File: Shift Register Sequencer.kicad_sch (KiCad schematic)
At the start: 103 parts, among them J1 Gate IN, J10 Step 4, J11 Step C, J12 Step 5, J13 Step F, J14 Step 0-F, J2 Step 0, J3 Step 6, J4 Step 1, J5 Step 7, J6 Step 2, J7 Step 8, J8 Step 3, J9 Step A, Q1 2N3904, Q2 2N3904, SW1 oneShot/continous, SW2 oneShot/continous, U1 4070, U2 SN74HC595N, U3 SN74HC595N, U4 TL072, U5 CD4050, U6 CD4050, U7 TL072

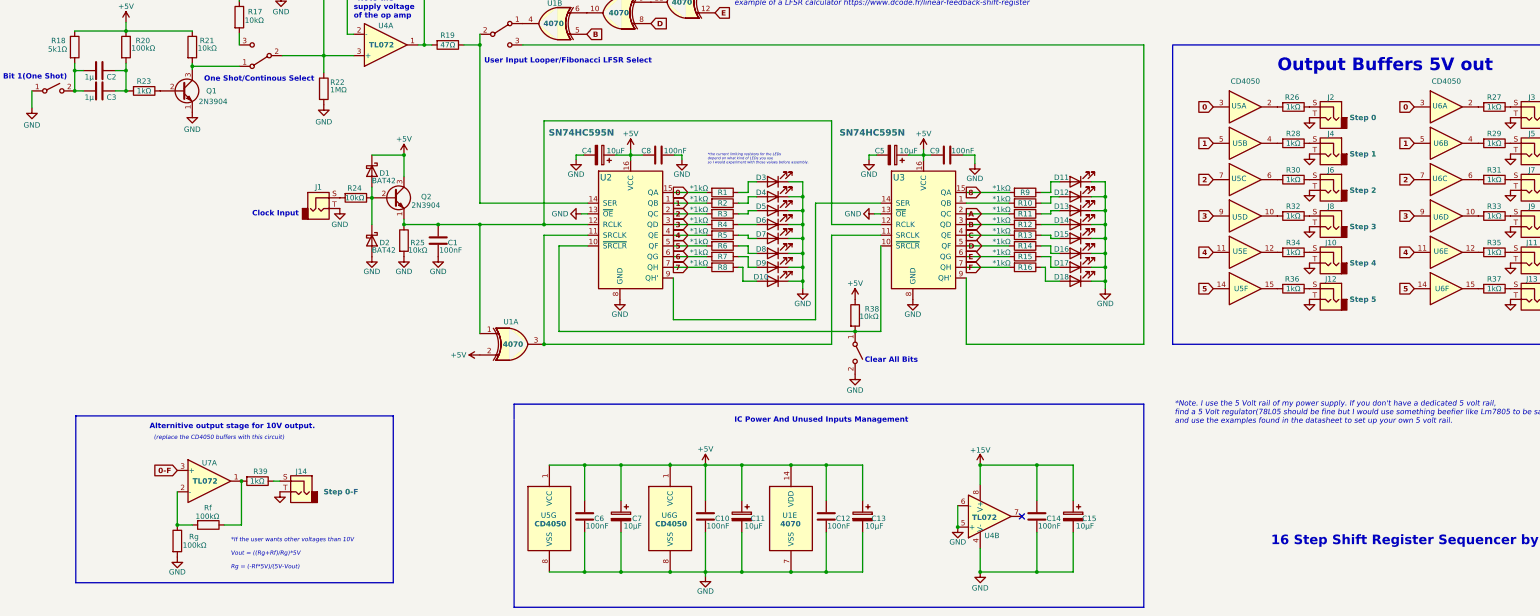
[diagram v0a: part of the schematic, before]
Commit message: Update Shift Register Sequencer.kicad_sch
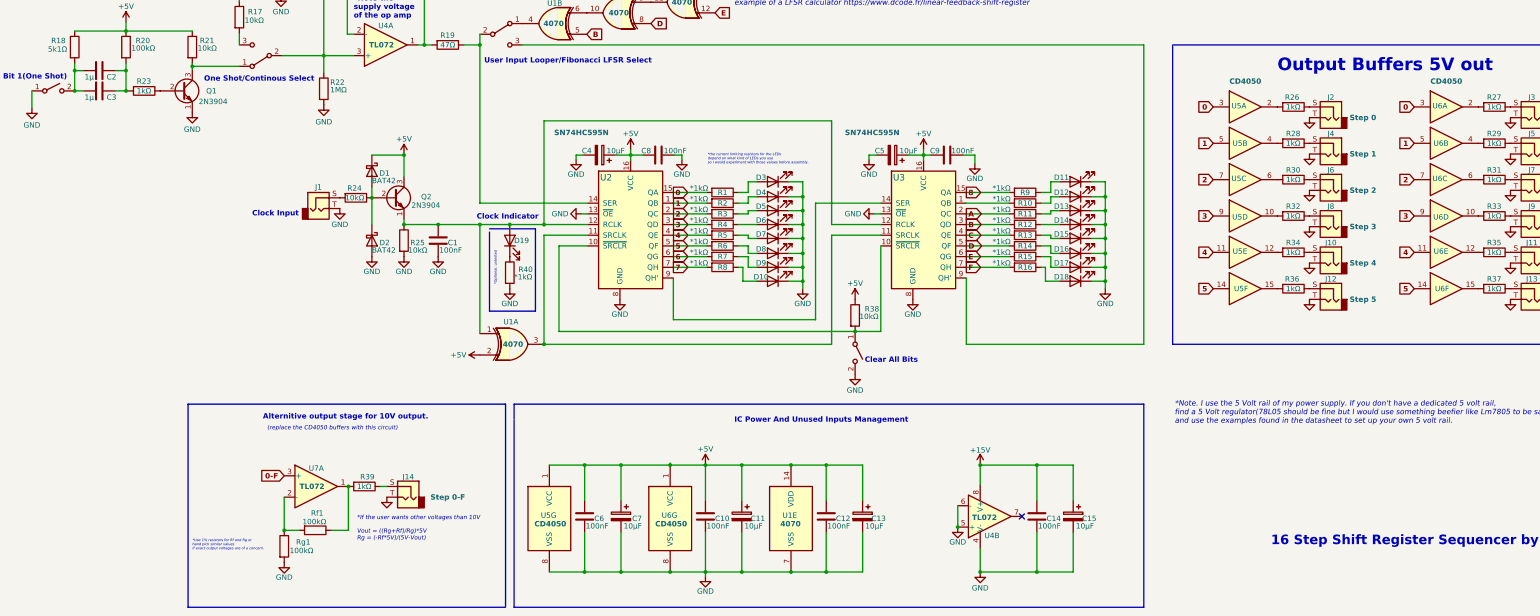
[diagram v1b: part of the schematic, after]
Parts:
- added D19: LED, LED_THT:LED_D3.0mm, symbol Device:LED
- added R40: *1kΩ, Resistor_THT:R_Axial_DIN0207_L6.3mm_D2.5mm_P7.62mm_Horizontal, symbol Device:R
- renumbered Rf to Rf1, Rg to Rg1
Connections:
- net GND: now also R40.2
- net at C1.1, Q2.1 (E), R25.1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: now also D19.2 (A)
- new net: D19.1 (K), R40.1
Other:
- note added: "*Optional, untested"
- note added: "*Use 1% resistors for Rf and Rg or hand pick similar values if exact output voltages are of a concern."
- note added: "Clock Indicator"
- moved on the sheet: J14, R39, Rf1, Rg1, U7A

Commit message: Update
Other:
- note added: "*The taps can be configured in other ways if the user wants. example of a LFSR calculator https://www.dcode.fr/linear-feedback-shift-register *Note. If the LFSR is omitted the unused inputs of the CD4070 must be tied to ground or +5V"
- note removed: "*The taps can be configured in other ways if the user wants. example of a LFSR calculator https://www.dcode.fr/linear-feedback-shift-register"
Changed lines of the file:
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@@
     (effects (font (size 1.27 1.27) (thickness 0.254) bold) (justify left bottom))
   )
-  (text "*The taps can be configured in other ways if the user wants.\nexample of a LFSR calculator https://www.dcode.fr/linear-feedback-shift-register"
-    (at 191.008 27.178 0)
+  (text "*The taps can be configured in other ways if the user wants.\nexample of a LFSR calculator https://www.dcode.fr/linear-feedback-shift-register\n\n*Note. If the LFSR is omitted the unused inputs of the CD4070 must be tied to ground or +5V "
+    (at 191.77 30.226 0)
     (effects (font (size 1.27 1.27) italic) (justify left bottom))
   )

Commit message: Added Trigger per Clock cycle option
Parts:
- removed U7: TL072, symbol Amplifier_Operational:TL072
- added C16, C18: 100nF, symbol Device:C
- added C17, C19: 10µF, symbol Device:C_Polarized
- added U7, U9: TL074, symbol Amplifier_Operational:TL074
- added U8: 4081, symbol 4xxx:4081
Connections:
- net +15V: now also C18.1, C19.1, U9.4 (V+)
- net +5V: now also C16.1, C17.1, U8.14 (VDD)
- net 0-F: now also U7.3 (+), U8.2
- net GND: now also C16.2, C17.2, C18.2, C19.2, U8.7 (VSS), U9.11 (V-)
- net Clock Out: now reaches C1.1, D19.2 (A), Q2.1 (E), R25.1, U1.1, U2.12 (RCLK), U3.12 (RCLK)
- net Clock Out: now also U8.1
- net at R39.2, Rf1.1: now also U7.1
- net at Rf1.2, Rg1.1: now also U7.2 (-)
- new net Buffer: U8.3
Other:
- note added: "*From Shift register outputs"
- note added: "*To CD4050/Op amp inputs"
- note added: "This mod sacrifices the gate option for a trigger on each clock."
- note added: "Trigger Modification"
- moved on the sheet: C10, C11, C12, C13, C14, C15, C6, C7, J14, R39, Rf1, Rg1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
